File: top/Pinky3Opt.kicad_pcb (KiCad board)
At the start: 2 copper layers, 136 x 112.7 mm, 33 parts

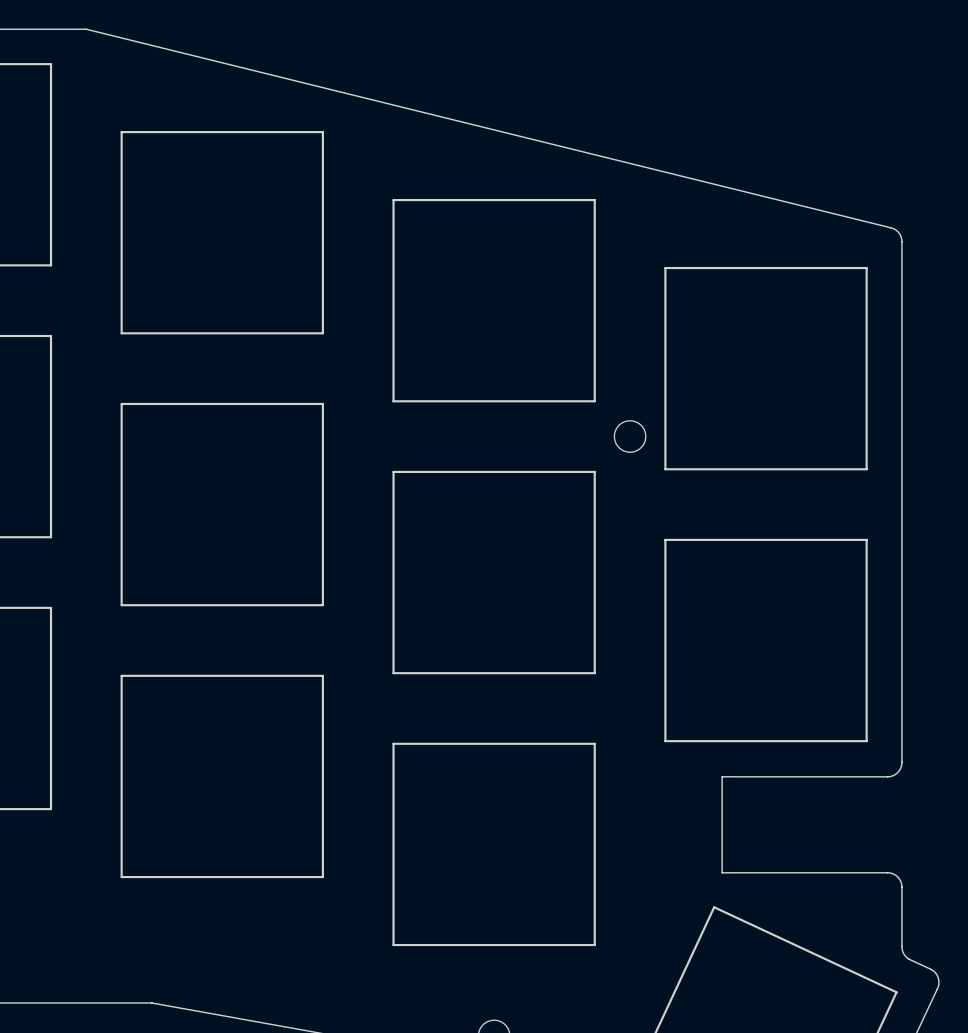
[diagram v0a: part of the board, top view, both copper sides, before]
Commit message: trrs bottom side
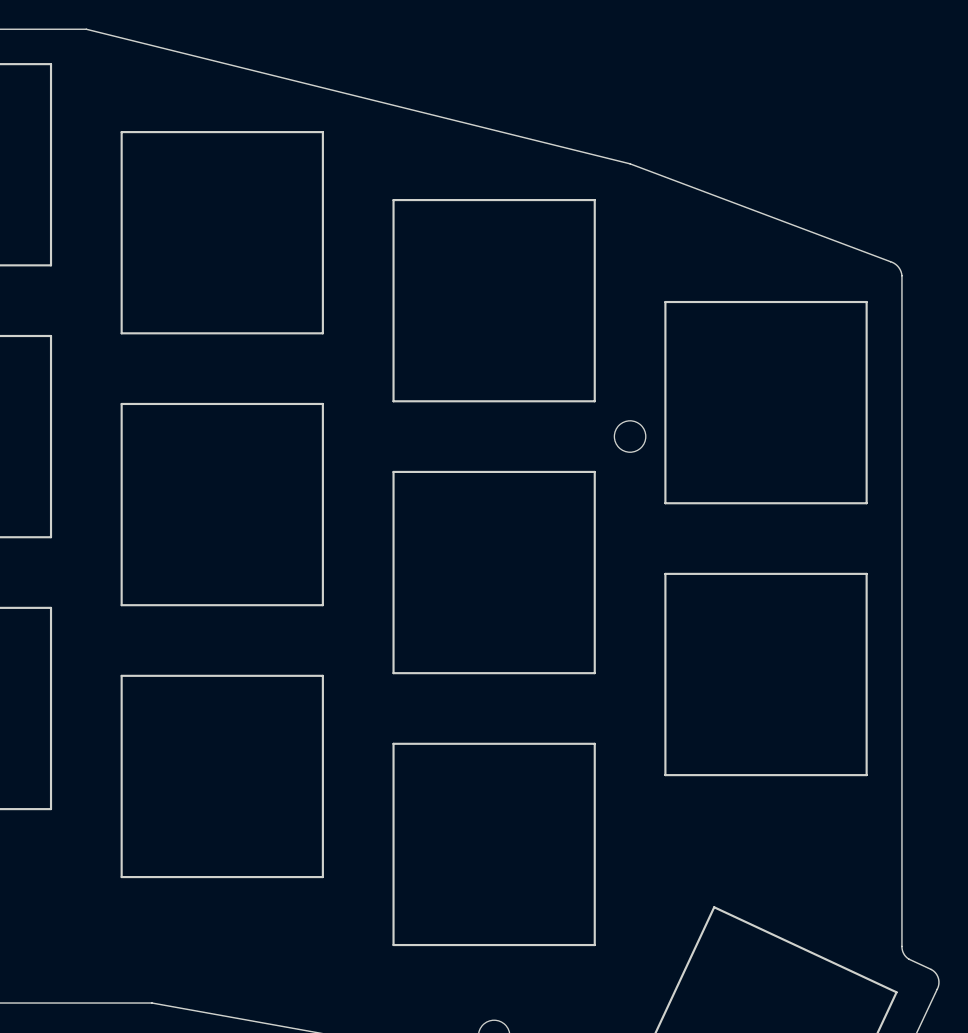
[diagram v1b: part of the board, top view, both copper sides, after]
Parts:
- moved MX14 2.38 mm to (152.4, 88.1)
- moved MX7 2.38 mm to (152.4, 69.1)
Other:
- outline, holes or cut-outs redrawn
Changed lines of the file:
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@@
   )
   (footprint "kbd_SW_Hole:SW_Hole_1u" (layer "F.Cu")
-    (at 152.4 66.675)
+    (at 152.4 69.05625)
     (property "Sheetfile" "Pinky3Opt.kicad_sch")
     (property "Sheetname" "")
@@
   )
   (footprint "kbd_SW_Hole:SW_Hole_1u" (layer "F.Cu")
-    (at 152.4 85.725)
+    (at 152.4 88.10625)
     (property "Sheetfile" "Pinky3Opt.kicad_sch")
     (property "Sheetname" "")
@@
   (gr_line (start 98.404 147.53125) (end 82.354 141.65625)
     (stroke (width 0.1) (type default)) (layer "Edge.Cuts"))
-  (gr_arc (start 161.124548 56.801362) (mid 161.699451 57.148616) (end 161.925 57.78125)
+  (gr_arc (start 161.124548 59.182612) (mid 161.674565 59.550194) (end 161.925 60.1625)
     (stroke (width 0.1) (type default)) (layer "Edge.Cuts"))
   (gr_line (start 91.975 111.125) (end 88.858243 111.125)
     (stroke (width 0.1) (type default)) (layer "Edge.Cuts"))
-  (gr_line (start 149.325 102) (end 160.900106 102)
-    (stroke (width 0.1) (type default)) (layer "Edge.Cuts"))
   (gr_line (start 53.925 122.075) (end 53.925 114.316233)
     (stroke (width 0.1) (type default)) (layer "Edge.Cuts"))
-  (gr_line (start 149.325 95.275) (end 149.325 102)
-    (stroke (width 0.1) (type default)) (layer "Edge.Cuts"))
   (gr_arc (start 29.575001 114.316233) (mid 28.860834 114.020416) (end 28.565017 113.306249)
     (stroke (width 0.1) (type default)) (layer "Edge.Cuts"))
   (gr_arc (start 28.565017 57.834528) (mid 28.775003 57.206252) (end 29.322857 56.833855)
     (stroke (width 0.1) (type default)) (layer "Edge.Cuts"))
-  (gr_line (start 161.925 102.991804) (end 161.925 107.163771)
-    (stroke (width 0.1) (type default)) (layer "Edge.Cuts"))
   (gr_line (start 98.475 111.125) (end 98.475 129.775)
     (stroke (width 0.1) (type default)) (layer "Edge.Cuts"))
@@
   (gr_line (start 155.948005 126.074218) (end 139.275 118.3)
     (stroke (width 0.1) (type default)) (layer "Edge.Cuts"))
-  (gr_line (start 104.775 42.89425) (end 161.124548 56.801362)
-    (stroke (width 0.1) (type default)) (layer "Edge.Cuts"))
-  (gr_arc (start 160.900106 102) (mid 161.61797 102.283632) (end 161.925 102.991804)
+  (gr_line (start 104.775 42.89425) (end 142.875 52.324)
     (stroke (width 0.1) (type default)) (layer "Edge.Cuts"))
   (gr_line (start 86.929 125.55) (end 67.204 122.075)
@@
   (gr_arc (start 157.099855 125.70331) (mid 156.6 126.125) (end 155.948005 126.074218)
     (stroke (width 0.1) (type default)) (layer "Edge.Cuts"))
-  (gr_line (start 161.925 57.78125) (end 161.925 94.244396)
+  (gr_line (start 161.925 60.1625) (end 161.925 107.163771)
     (stroke (width 0.1) (type default)) (layer "Edge.Cuts"))
   (gr_line (start 45.962237 137.687039) (end 45.962236 123.099689)
@@
   (gr_line (start 120.921697 142.43047) (end 113.511748 155.169705)
     (stroke (width 0.1) (type default)) (layer "Edge.Cuts"))
-  (gr_arc (start 161.925 94.244396) (mid 161.636192 94.96929) (end 160.919388 95.277632)
-    (stroke (width 0.1) (type default)) (layer "Edge.Cuts"))
   (gr_line (start 53.925 114.316233) (end 29.575001 114.316233)
     (stroke (width 0.1) (type default)) (layer "Edge.Cuts"))
@@
   (gr_line (start 60.375 122.075) (end 60.375 114.316233)
     (stroke (width 0.1) (type default)) (layer "Edge.Cuts"))
-  (gr_line (start 160.919388 95.277632) (end 149.325 95.275)
+  (gr_line (start 142.875 52.324) (end 161.124548 59.182612)
     (stroke (width 0.1) (type default)) (layer "Edge.Cuts"))
   (gr_line (start 82.354 141.65625) (end 65.504 138.691681)
